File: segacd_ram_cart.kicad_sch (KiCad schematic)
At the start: 16 parts, among them J1 Sega_MegaDrive_Cart_Conn, J2 AVR-JTAG-10, J3 Backup, U1 CY62148ELL-45ZSXI, U2 BQ2201SN, U3 ATF1502AS-xAx44

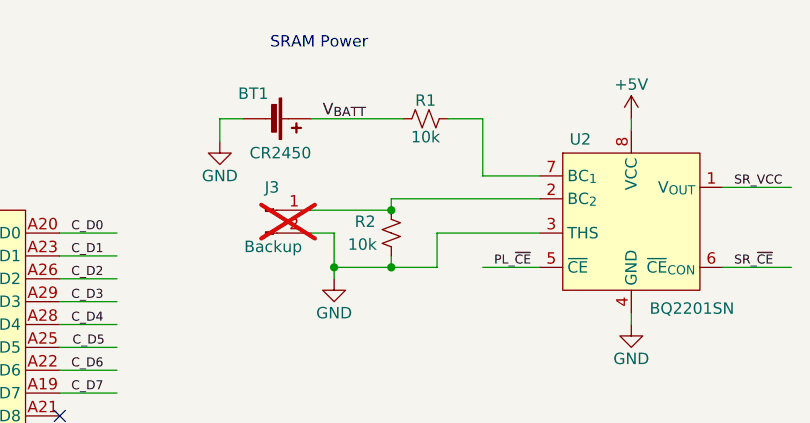
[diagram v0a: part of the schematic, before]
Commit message: Changed layout and updated symbols/footprints
* Changed the layout of components to allow for shrinking the board.
* Imported custom symbols and footprints into project library.
* Updated symbols and footprints to satisfy ERC/DRC checks.
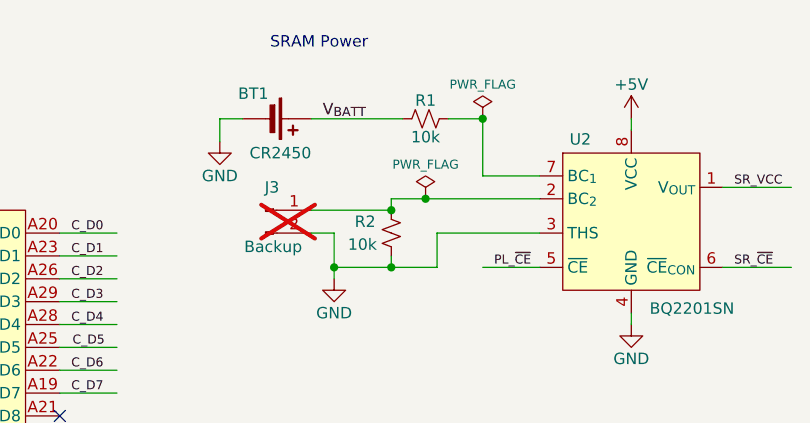
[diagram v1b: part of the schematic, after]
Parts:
- J1: footprint My_Library:2x32_P2.54mm_Edge -> Custom:2x32_P2.54mm_Edge; symbol My_Library:Sega_MegaDrive_Cart_Conn -> Custom:Sega_MegaDrive_Cart_Conn
- U1: symbol My_Library_7:CY62138ELL-45ZSXI -> Custom:CY62138ELL-45ZSXI
- U2: symbol My_Library_7:BQ2201SN -> Custom:BQ2201SN
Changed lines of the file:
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@@
 	)
 	(junction
+		(at 101.6 34.29)
+		(diameter 0)
+		(color 0 0 0 0)
+	)
+	(junction
 		(at 212.09 27.94)
 		(diameter 0)
@@
 	)
 	(junction
+		(at 107.95 25.4)
+		(diameter 0)
+		(color 0 0 0 0)
+	)
+	(junction
 		(at 97.79 35.56)
 		(diameter 0)
@@
 	(wire
 		(pts
-			(xy 114.3 34.29) (xy 97.79 34.29)
+			(xy 114.3 34.29) (xy 101.6 34.29)
 		)
 		(stroke
@@
 	(wire
 		(pts
+			(xy 101.6 34.29) (xy 97.79 34.29)
+		)
+		(stroke
+			(width 0)
+			(type default)
+		)
+	)
+	(wire
+		(pts
 			(xy 102.87 41.91) (xy 97.79 41.91)
 		)
@@
 	)
 	(symbol
-		(lib_id "My_Library:Sega_MegaDrive_Cart_Conn")
+		(lib_id "Custom:Sega_MegaDrive_Cart_Conn")
 		(at 49.53 76.2 0)
 		(unit 1)
@@
 			)
 		)
-		(property "Footprint" "My_Library:2x32_P2.54mm_Edge"
+		(property "Footprint" "Custom:2x32_P2.54mm_Edge"
 			(at 31.75 124.46 0)
 			(effects
@@
 		)
 		(property "Datasheet" ""
-			(at 49.53 71.12 0)
+			(at 52.07 71.12 0)
 			(effects
 				(font
@@
 			)
 		)
-		(property "Description" ""
+		(property "Description" "Sega Mega Drive Cartridge Connector"
 			(at 49.53 76.2 0)
 			(effects
@@
 	)
 	(symbol
+		(lib_id "power:PWR_FLAG")
+		(at 101.6 34.29 0)
+		(unit 1)
+		(exclude_from_sim no)
+		(in_bom yes)
+		(on_board yes)
+		(dnp no)
+		(property "Reference" "#FLG02"
+			(at 101.6 32.385 0)
+			(effects
+				(font
+					(size 1.27 1.27)
+				)
+				(hide yes)
+			)
+		)
+		(property "Value" "PWR_FLAG"
+			(at 101.6 30.48 0)
+			(effects
+				(font
+					(size 1 1)
+				)
+			)
+		)
+		(property "Footprint" ""
+			(at 101.6 34.29 0)
+			(effects
+				(font
+					(size 1.27 1.27)
+				)
+				(hide yes)
+			)
+		)
+		(property "Datasheet" "~"
+			(at 101.6 34.29 0)
+			(effects
+				(font
+					(size 1.27 1.27)
+				)
+				(hide yes)
+			)
+		)
+		(property "Description" "Special symbol for telling ERC where power comes from"
+			(at 101.6 34.29 0)
+			(effects
+				(font
+					(size 1.27 1.27)
+				)
+				(hide yes)
+			)
+		)
+		(pin "1"
+		)
+		(instances
+			(project "segacd_ram_cart"
+				(path "/e945ae1e-7690-4b90-bf05-83f0d799da55"
+					(reference "#FLG02")
+					(unit 1)
+				)
+			)
+		)
+	)
+	(symbol
 		(lib_id "Device:C_Small")
 		(at 205.74 31.75 0)
@@
 	)
 	(symbol
+		(lib_id "power:PWR_FLAG")
+		(at 107.95 25.4 0)
+		(unit 1)
+		(exclude_from_sim no)
+		(in_bom yes)
+		(on_board yes)
+		(dnp no)
+		(property "Reference" "#FLG01"
+			(at 107.95 23.495 0)
+			(effects
+				(font
+					(size 1.27 1.27)
+				)
+				(hide yes)
+			)
+		)
+		(property "Value" "PWR_FLAG"
+			(at 107.95 21.59 0)
+			(effects
+				(font
+					(size 1 1)
+				)
+			)
+		)
+		(property "Footprint" ""
+			(at 107.95 25.4 0)
+			(effects
+				(font
+					(size 1.27 1.27)
+				)
+				(hide yes)
+			)
+		)
+		(property "Datasheet" "~"
+			(at 107.95 25.4 0)
+			(effects
+				(font
+					(size 1.27 1.27)
+				)
+				(hide yes)
+			)
+		)
+		(property "Description" "Special symbol for telling ERC where power comes from"
+			(at 107.95 25.4 0)
+			(effects
+				(font
+					(size 1.27 1.27)
+				)
+				(hide yes)
+			)
+		)
+		(pin "1"
+		)
+		(instances
+			(project ""
+				(path "/e945ae1e-7690-4b90-bf05-83f0d799da55"
+					(reference "#FLG01")
+					(unit 1)
+				)
+			)
+		)
+	)
+	(symbol
 		(lib_id "power:GND")
 		(at 49.53 128.27 0)
@@
 			)
 		)
-		(property "Description" ""
+		(property "Description" "Power symbol creates a global label with name \"GND\" , ground"
 			(at 49.53 128.27 0)
 			(effects
@@
 			)
 		)
-		(property "Description" ""
+		(property "Description" "Power symbol creates a global label with name \"+5V\""
 			(at 124.46 25.4 0)
 			(effects
@@
 			)
 		)
-		(property "Description" ""
+		(property "Description" "Power symbol creates a global label with name \"+5V\""
 			(at 163.195 26.67 0)
 			(effects
@@
 			)
 		)
-		(property "Description" ""
+		(property "Description" "Power symbol creates a global label with name \"GND\" , ground"
 			(at 78.74 27.94 0)
 			(effects
@@
 			)
 		)
-		(property "Description" ""
+		(property "Description" "Power symbol creates a global label with name \"GND\" , ground"
 			(at 199.39 36.83 0)
 			(effects
@@
 	)
 	(symbol
-		(lib_id "My_Library_7:BQ2201SN")
+		(lib_id "Custom:BQ2201SN")
 		(at 124.46 36.83 0)
 		(unit 1)
@@
 			)
 		)
-		(property "Description" ""
+		(property "Description" "Power symbol creates a global label with name \"+5V\""
 			(at 195.58 69.85 0)
 			(effects
@@
 			)
 		)
-		(property "Description" ""
+		(property "Description" "Power symbol creates a global label with name \"GND\" , ground"
 			(at 124.46 48.26 0)
 			(effects
@@
 			)
 		)
-		(property "Description" ""
+		(property "Description" "Power symbol creates a global label with name \"GND\" , ground"
 			(at 195.58 128.27 0)
 			(effects
@@
 			)
 		)
-		(property "Description" ""
+		(property "Description" "Power symbol creates a global label with name \"GND\" , ground"
 			(at 48.895 180.34 0)
 			(effects
@@
 			)
 		)
-		(property "Description" ""
+		(property "Description" "Power symbol creates a global label with name \"GND\" , ground"
 			(at 187.96 36.83 0)
 			(effects
@@
 			)
 		)
-		(property "Description" ""
+		(property "Description" "Power symbol creates a global label with name \"GND\" , ground"
 			(at 91.44 43.18 0)
 			(effects
@@
 			)
 		)
-		(property "Description" ""
+		(property "Description" "Single-cell battery"
 			(at 83.82 25.4 0)
 			(effects
@@
 			)
 		)
-		(property "Description" ""
+		(property "Description" "Power symbol creates a global label with name \"GND\" , ground"
 			(at 118.11 137.16 0)
 			(effects
@@
 			)
 		)
-		(property "Description" ""
+		(property "Description" "Power symbol creates a global label with name \"+5V\""
 			(at 49.53 29.21 0)
 			(effects
@@
 			)
 		)
-		(property "Description" ""
+		(property "Description" "Power symbol creates a global label with name \"+5V\""
 			(at 199.39 26.67 0)
 			(effects
@@
 			)
 		)
-		(property "Datasheet" " ~"
+		(property "Datasheet" "~"
 			(at 16.51 177.8 0)
 			(effects
@@
 			)
 		)
-		(property "Description" ""
+		(property "Description" "Atmel 10-pin JTAG connector"
 			(at 48.895 163.83 0)
 			(effects
@@
 			)
 		)
-		(property "Description" ""
+		(property "Description" "Power symbol creates a global label with name \"GND\" , ground"
 			(at 163.195 36.83 0)
 			(effects
@@
 			)
 		)
-		(property "Description" ""
+		(property "Description" "Power symbol creates a global label with name \"+5V\""
 			(at 46.355 147.32 0)
 			(effects
@@
 	)
 	(symbol
-		(lib_id "My_Library_7:CY62138ELL-45ZSXI")
+		(lib_id "Custom:CY62138ELL-45ZSXI")
 		(at 118.11 101.6 0)
 		(unit 1)
